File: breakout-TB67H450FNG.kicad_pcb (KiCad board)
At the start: 2 copper layers, 5 parts, among them IC1 TB67H450FNG,EL

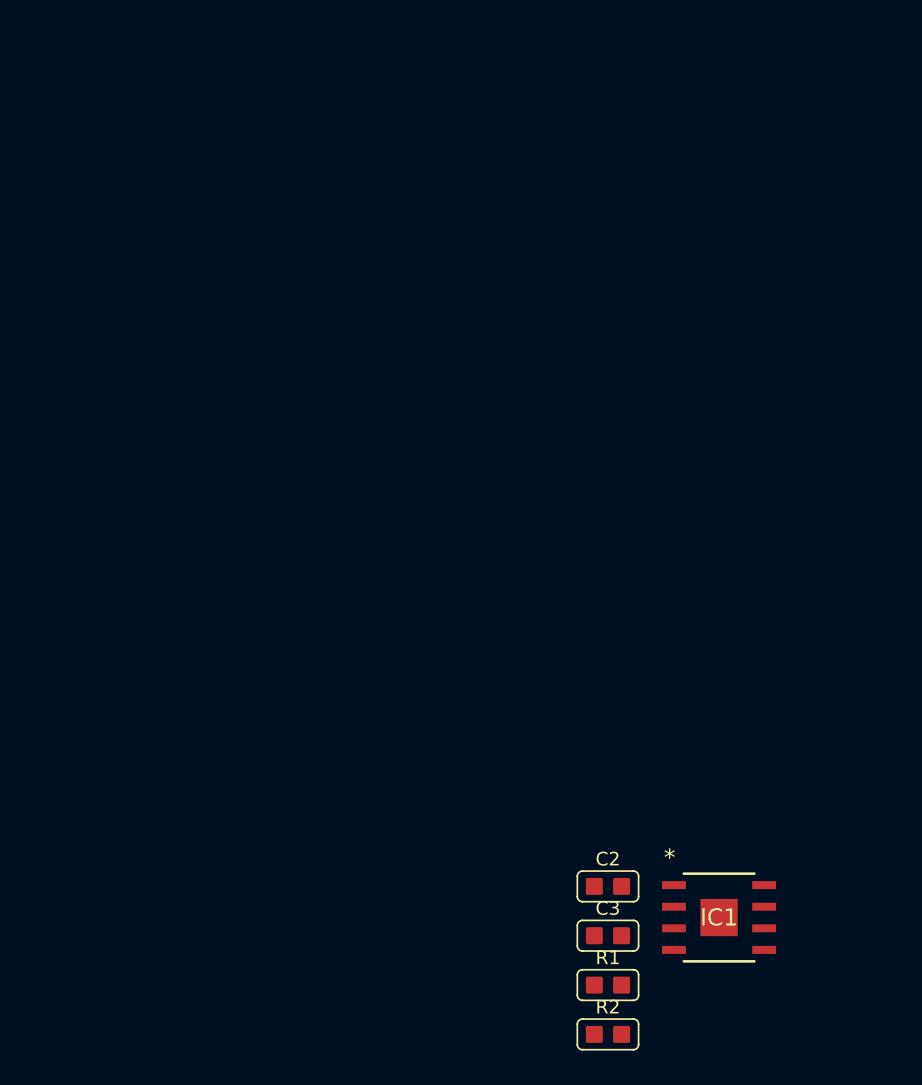
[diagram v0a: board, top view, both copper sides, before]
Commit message: Changed Footpint, Added DEBUG LED, Layouted PCB
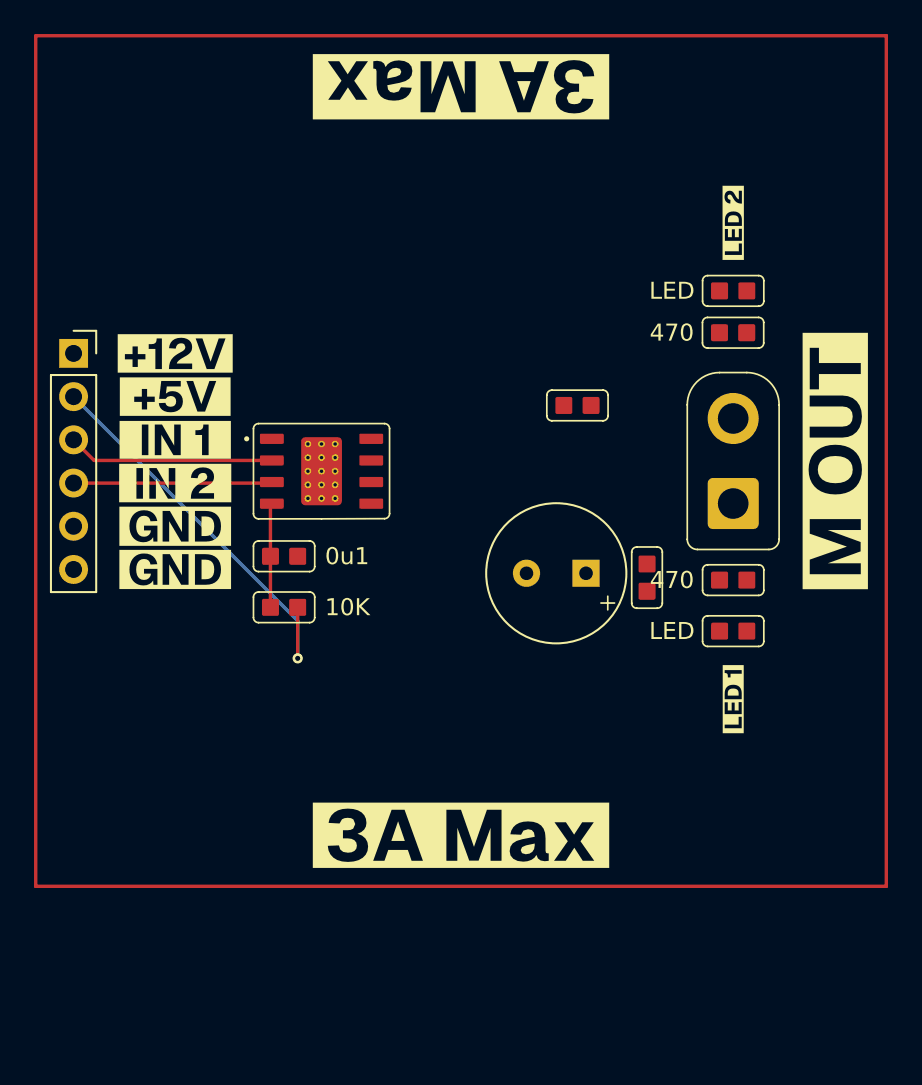
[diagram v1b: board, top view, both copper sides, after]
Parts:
- added C1: 100u, breakout-TB67H450FNG:CP_Radial_D8.0mm_P3.50mm, F.Cu at (55.6, 56.6)
- added D1: LED, breakout-TB67H450FNG:led0603, F.Cu at (66.0, 60.0)
- added D2: LED, breakout-TB67H450FNG:led0603, F.Cu at (66.0, 40.0)
- added J1: Conn_01x06, Connector_PinSocket_2.54mm:PinSocket_1x06_P2.54mm_Vertical, F.Cu at (27.2, 43.7)
- added J2: Screw_Terminal_01x02, breakout-TB67H450FNG:xt30-f, F.Cu at (66.0, 50.0)
- added R3: 470, breakout-TB67H450FNG:res0603, F.Cu at (66.0, 57.0)
- added R4: 470, breakout-TB67H450FNG:res0603, F.Cu at (66.0, 42.5)
- added kibuzzard-66A14E1C: G***, kibuzzard-66A14E1C, F.Cu at (72.0, 50.0)
- added kibuzzard-66A14E66: G***, kibuzzard-66A14E66, F.Cu at (66.0, 36.0)
- added kibuzzard-66A14E76: G***, kibuzzard-66A14E76, F.Cu at (66.0, 64.0)
- added kibuzzard-66A14E9E: G***, kibuzzard-66A14E9E, F.Cu at (50.0, 72.0)
- added kibuzzard-66A14EA3: G***, kibuzzard-66A14EA3, F.Cu at (50.0, 28.0)
- added kibuzzard-66A15010: G***, kibuzzard-66A15010, F.Cu at (33.2, 53.8)
- added kibuzzard-66A15016: G***, kibuzzard-66A15016, F.Cu at (33.2, 56.4)
- added kibuzzard-66A15073: G***, kibuzzard-66A15073, F.Cu at (33.2, 51.3)
- added kibuzzard-66A15093: G***, kibuzzard-66A15093, F.Cu at (33.2, 48.8)
- added kibuzzard-66A150A6: G***, kibuzzard-66A150A6, F.Cu at (33.2, 46.2)
- added kibuzzard-66A150AD: G***, kibuzzard-66A150AD, F.Cu at (33.2, 43.7)
- moved R2 37.0 mm to (56.8, 46.7)
- moved IC1 35.1 mm to (41.8, 50.6)
- moved C3 29.3 mm to (39.6, 55.6)
- moved R1 29.2 mm to (39.6, 58.6), turned to 180 degrees
- moved C2 18.3 mm to (60.9, 56.9), turned to -90 degrees
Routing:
- net +5V: track 0.00 -> 23.8 mm, vias 0 -> 1
- net /M IN 2: track 0.00 -> 12.2 mm
- net /M IN 1: track 0.00 -> 11.7 mm
- net Net-(IC1-VREF): track 0.00 -> 6.24 mm

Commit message: Almost close to finishing
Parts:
- added H1: MountingHole_Pad, MountingHole:MountingHole_3.2mm_M3_Pad_Via, F.Cu at (28.8, 28.8)
- added H2: MountingHole_Pad, MountingHole:MountingHole_3.2mm_M3_Pad_Via, F.Cu at (71.2, 28.8)
- added H3: MountingHole_Pad, MountingHole:MountingHole_3.2mm_M3_Pad_Via, F.Cu at (28.8, 71.2)
- added H4: MountingHole_Pad, MountingHole:MountingHole_3.2mm_M3_Pad_Via, F.Cu at (71.2, 71.2)
- moved C2 13.7 mm to (47.2, 57.2)
- moved R2 12.2 mm to (44.8, 45.0), turned to 90 degrees
- moved C1 1.71 mm to (54.0, 57.2), turned to -90 degrees
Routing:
- net /M OUT 2: track 0.00 -> 27.1 mm
- net /M OUT 1: track 0.00 -> 26.6 mm
- net Net-(IC1-RS): track 0.00 -> 8.58 mm, vias 0 -> 2
- net +5V: track 23.8 -> 27.0 mm
- net Net-(D1-A): track 0.00 -> 3.00 mm
- net Net-(D2-A): track 0.00 -> 2.46 mm
- added copper zone on B.Cu, net +12V
- added copper zone on F.Cu, net +12V
- added copper zone on B.Cu, net GND
- added copper zone on F.Cu, net GND
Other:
- board outline added: 50 x 50 mm

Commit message: Gerber
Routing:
- net /M OUT 2: track 27.1 -> 26.0 mm
- net /M OUT 1: track 26.6 -> 25.5 mm
